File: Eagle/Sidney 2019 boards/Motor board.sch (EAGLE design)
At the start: 41 parts, among them IC2 LM2940CS-5.0_NOPB, IC3 LM3940IS-3.3

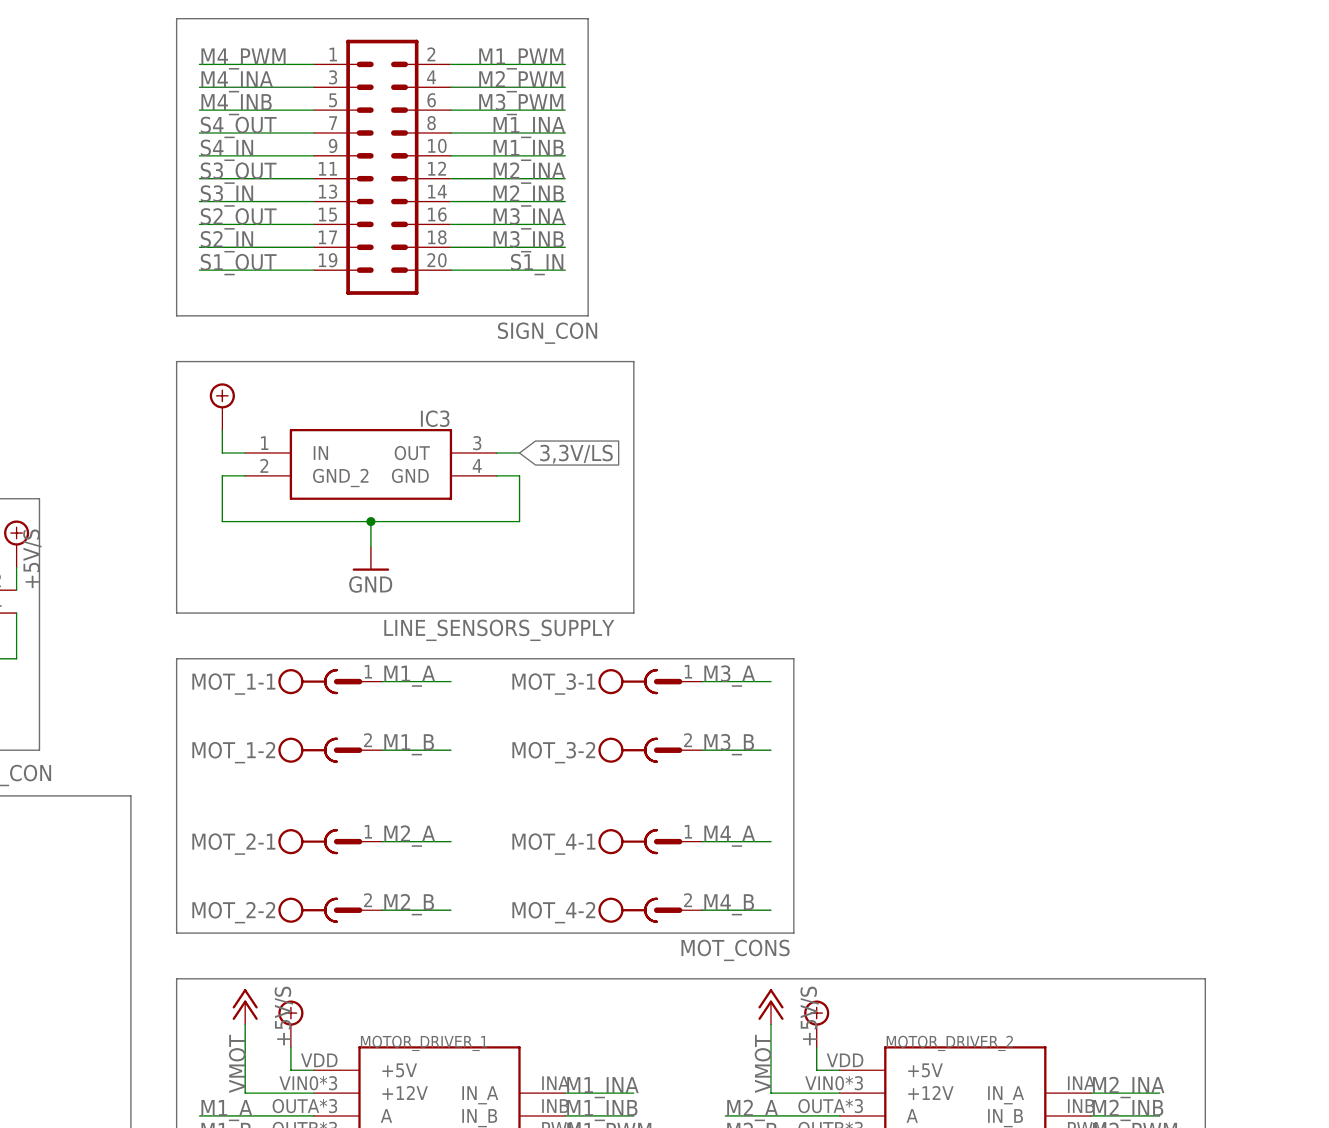
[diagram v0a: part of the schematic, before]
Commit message: Working on vias, removed empty portions of the motor board, added 3,3V LDO regulator for line sensors
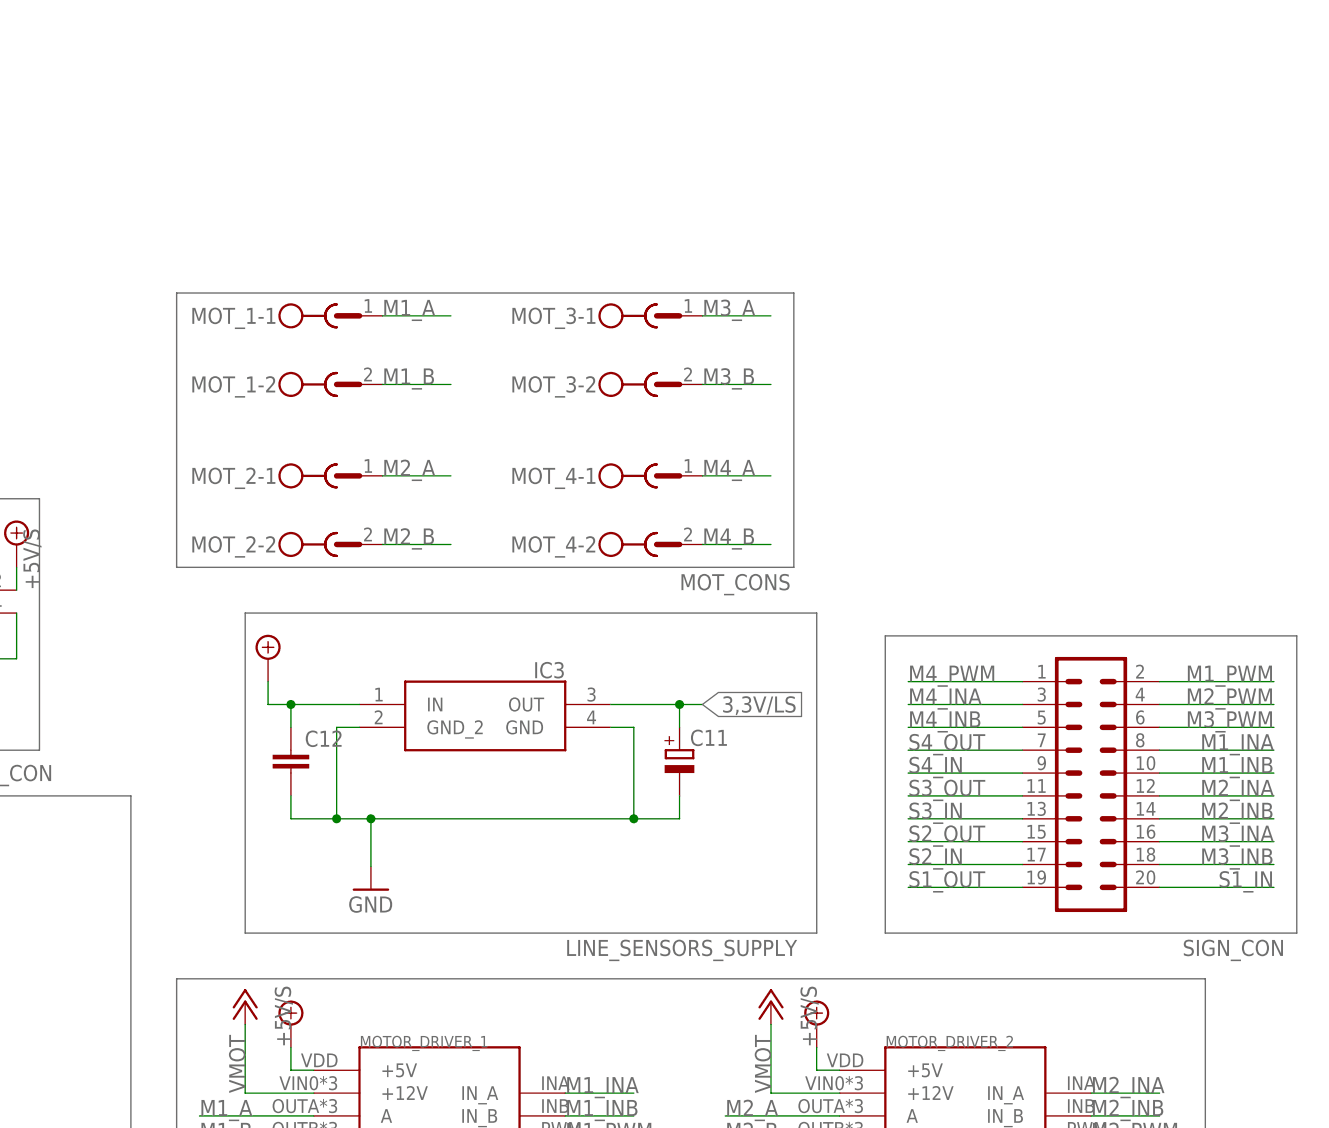
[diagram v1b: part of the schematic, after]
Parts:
- added C11: (no value), rcl:CPOL-EUE
- added C12: 100nF, rcl:C-EUC1206
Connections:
- net +5V/S: now also C12.1
- net 3,3V/LS: now also C11.+
- net GND: now also C11.-, C12.2
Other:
- moved on the sheet: IC3, MOT_1-1, MOT_1-2, MOT_2-1, MOT_2-2, MOT_3-1, MOT_3-2, MOT_4-1, MOT_4-2, SIGN_CON
